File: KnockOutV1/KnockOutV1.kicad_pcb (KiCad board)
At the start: 2 copper layers, 1 part

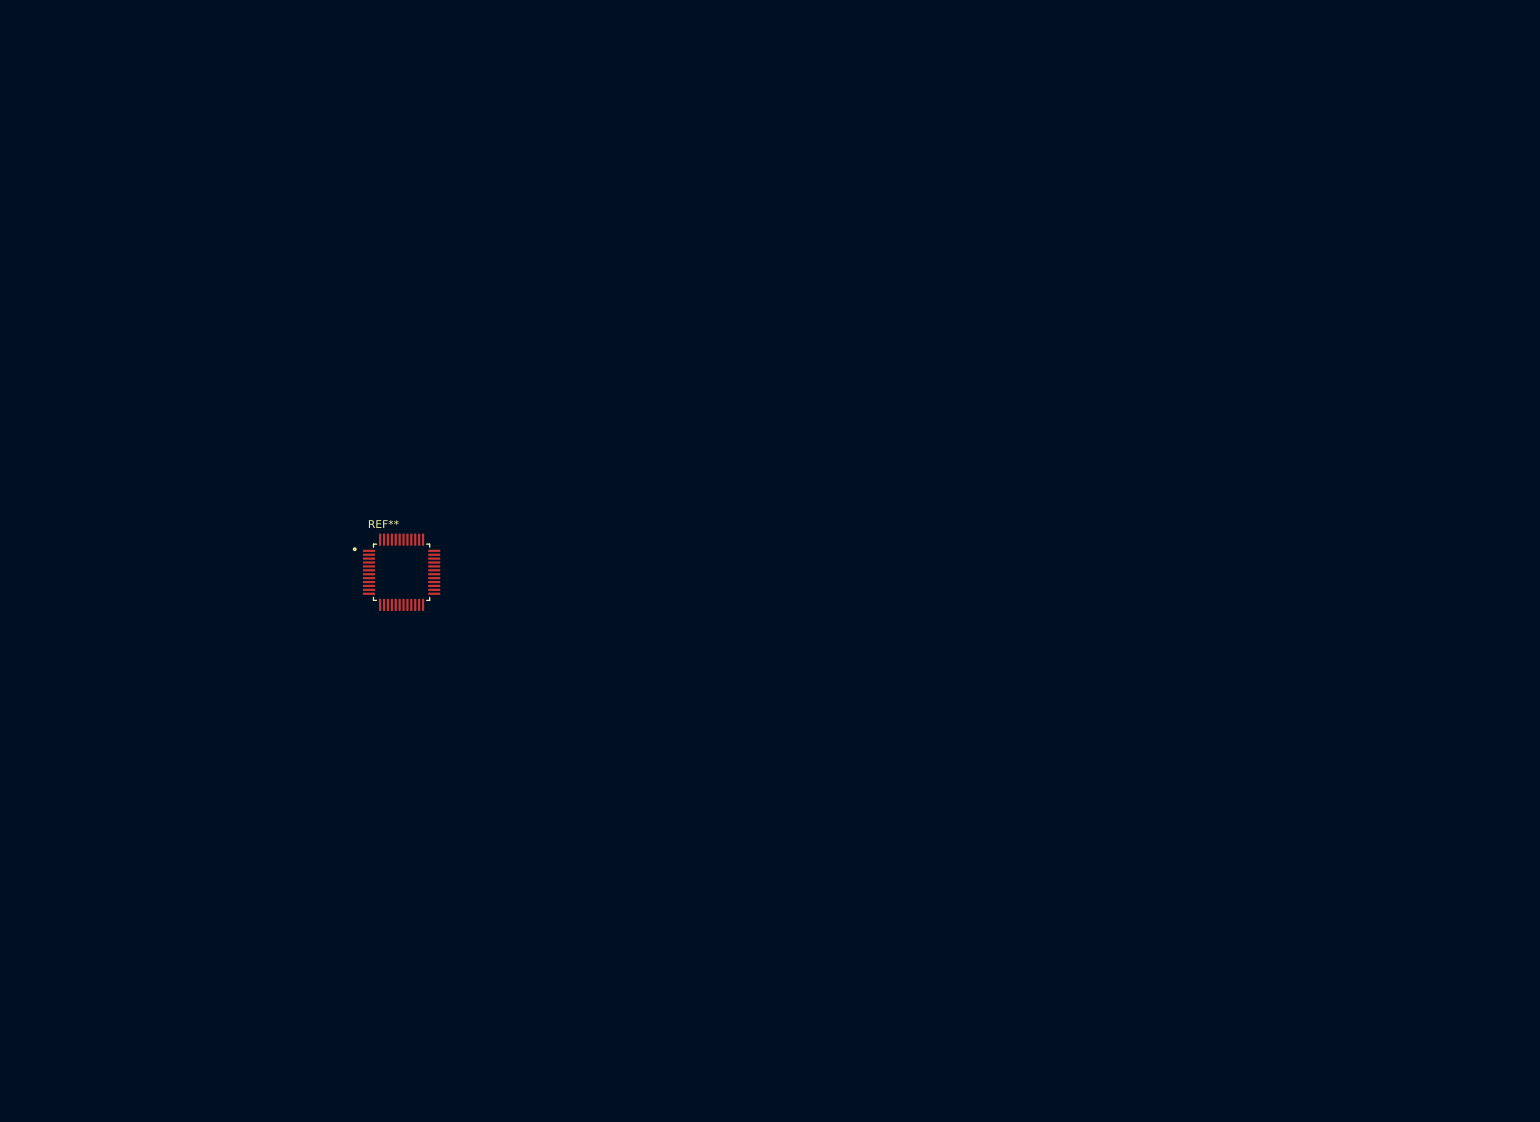
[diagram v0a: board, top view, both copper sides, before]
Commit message: Began Schematic Pin Breakout
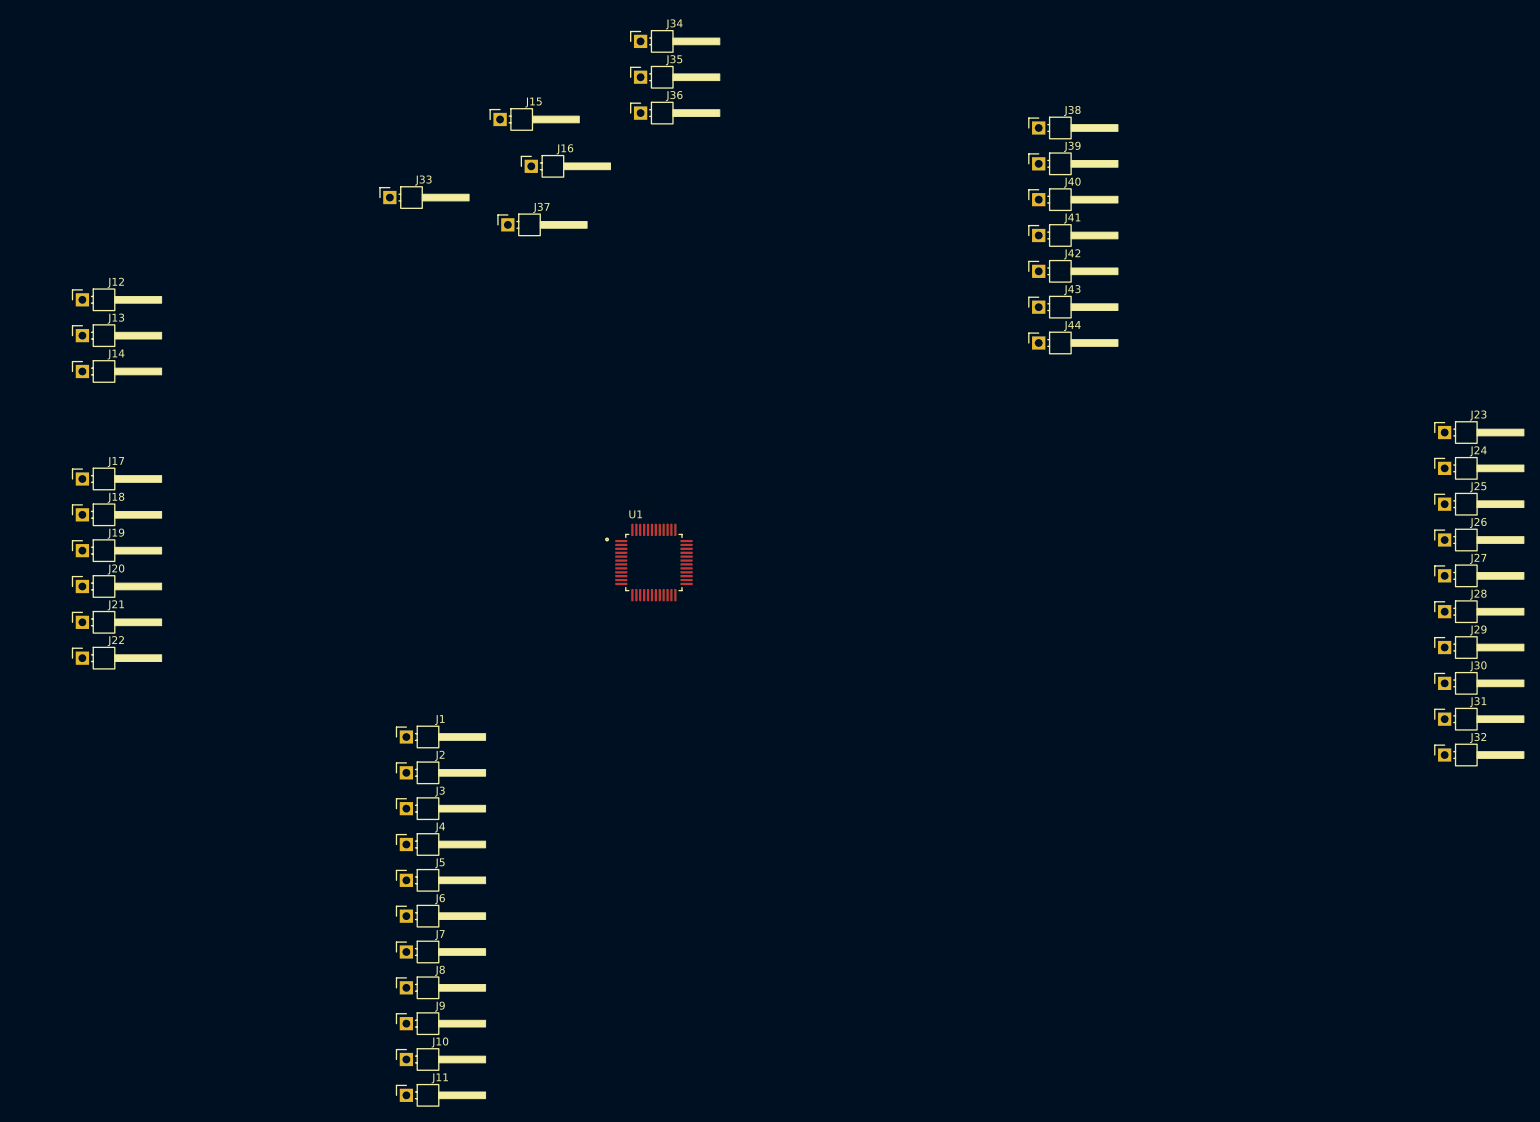
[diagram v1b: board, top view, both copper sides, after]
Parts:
- removed REF**: QFP50P900X900X160-48N, STM32F103C8T6:QFP50P900X900X160-48N
- added J1: Conn1x1Pin-PA0_WKUP, Connector_PinHeader_2.54mm:PinHeader_1x01_P2.54mm_Horizontal, F.Cu at (110.1, 109.6)
- added J10: Conn1x1Pin-PA9, Connector_PinHeader_2.54mm:PinHeader_1x01_P2.54mm_Horizontal, F.Cu at (110.1, 150.9)
- added J11: Conn1x1Pin-PA10, Connector_PinHeader_2.54mm:PinHeader_1x01_P2.54mm_Horizontal, F.Cu at (110.1, 155.5)
- added J12: Conn1x1Pin-PA11, Connector_PinHeader_2.54mm:PinHeader_1x01_P2.54mm_Horizontal, F.Cu at (68.6, 53.6)
- added J13: Conn1x1Pin-PA12, Connector_PinHeader_2.54mm:PinHeader_1x01_P2.54mm_Horizontal, F.Cu at (68.6, 58.2)
- added J14: Conn1x1Pin-PA13, Connector_PinHeader_2.54mm:PinHeader_1x01_P2.54mm_Horizontal, F.Cu at (68.6, 62.8)
- added J15: Conn1x1Pin-PA14, Connector_PinHeader_2.54mm:PinHeader_1x01_P2.54mm_Horizontal, F.Cu at (122.1, 30.5)
- added J16: Conn1x1Pin-PA15, Connector_PinHeader_2.54mm:PinHeader_1x01_P2.54mm_Horizontal, F.Cu at (126.1, 36.5)
- added J17: Conn1x1Pin-PC13-TAMPER-RTC, Connector_PinHeader_2.54mm:PinHeader_1x01_P2.54mm_Horizontal, F.Cu at (68.6, 76.5)
- added J18: Conn1x1Pin-PC14-OSC32_IN, Connector_PinHeader_2.54mm:PinHeader_1x01_P2.54mm_Horizontal, F.Cu at (68.6, 81.1)
- added J19: Conn1x1Pin-PC15-OSC32_OUT, Connector_PinHeader_2.54mm:PinHeader_1x01_P2.54mm_Horizontal, F.Cu at (68.6, 85.7)
- added J2: Conn1x1Pin-PA1, Connector_PinHeader_2.54mm:PinHeader_1x01_P2.54mm_Horizontal, F.Cu at (110.1, 114.2)
- added J20: Conn1x1Pin-VBAT, Connector_PinHeader_2.54mm:PinHeader_1x01_P2.54mm_Horizontal, F.Cu at (68.6, 90.3)
- added J21: Conn1x1Pin-NRST, Connector_PinHeader_2.54mm:PinHeader_1x01_P2.54mm_Horizontal, F.Cu at (68.6, 94.9)
- added J22: BOOT0, Connector_PinHeader_2.54mm:PinHeader_1x01_P2.54mm_Horizontal, F.Cu at (68.6, 99.5)
- added J23: Conn1x1Pin-VDD, Connector_PinHeader_2.54mm:PinHeader_1x01_P2.54mm_Horizontal, F.Cu at (243.1, 70.6)
- added J24: Conn1x1Pin-VDDA, Connector_PinHeader_2.54mm:PinHeader_1x01_P2.54mm_Horizontal, F.Cu at (243.1, 75.2)
- added J25: Conn1x1Pin-PB15, Connector_PinHeader_2.54mm:PinHeader_1x01_P2.54mm_Horizontal, F.Cu at (243.1, 79.8)
- added J26: Conn1x1Pin-PB14, Connector_PinHeader_2.54mm:PinHeader_1x01_P2.54mm_Horizontal, F.Cu at (243.1, 84.4)
- added J27: Conn1x1Pin-PB13, Connector_PinHeader_2.54mm:PinHeader_1x01_P2.54mm_Horizontal, F.Cu at (243.1, 89.0)
- added J28: Conn1x1Pin-PB12, Connector_PinHeader_2.54mm:PinHeader_1x01_P2.54mm_Horizontal, F.Cu at (243.1, 93.5)
- added J29: Conn1x1Pin-PB11, Connector_PinHeader_2.54mm:PinHeader_1x01_P2.54mm_Horizontal, F.Cu at (243.1, 98.1)
- added J3: Conn1x1Pin-PA2, Connector_PinHeader_2.54mm:PinHeader_1x01_P2.54mm_Horizontal, F.Cu at (110.1, 118.8)
- added J30: Conn1x1Pin-PB10, Connector_PinHeader_2.54mm:PinHeader_1x01_P2.54mm_Horizontal, F.Cu at (243.1, 102.7)
- added J31: Conn1x1Pin-PB9, Connector_PinHeader_2.54mm:PinHeader_1x01_P2.54mm_Horizontal, F.Cu at (243.1, 107.3)
- added J32: Conn1x1Pin-PB8, Connector_PinHeader_2.54mm:PinHeader_1x01_P2.54mm_Horizontal, F.Cu at (243.1, 111.9)
- added J33: Conn1x1Pin-PB7, Connector_PinHeader_2.54mm:PinHeader_1x01_P2.54mm_Horizontal, F.Cu at (108.0, 40.5)
- added J34: Conn1x1Pin-PB6, Connector_PinHeader_2.54mm:PinHeader_1x01_P2.54mm_Horizontal, F.Cu at (140.1, 20.5)
- added J35: Conn1x1Pin-PB5, Connector_PinHeader_2.54mm:PinHeader_1x01_P2.54mm_Horizontal, F.Cu at (140.1, 25.1)
- added J36: Conn1x1Pin-PB4, Connector_PinHeader_2.54mm:PinHeader_1x01_P2.54mm_Horizontal, F.Cu at (140.1, 29.7)
- added J37: Conn1x1Pin-PB3, Connector_PinHeader_2.54mm:PinHeader_1x01_P2.54mm_Horizontal, F.Cu at (123.1, 44.0)
- added J38: Conn1x1Pin-PB2, Connector_PinHeader_2.54mm:PinHeader_1x01_P2.54mm_Horizontal, F.Cu at (191.1, 31.6)
- added J39: Conn1x1Pin-PB1, Connector_PinHeader_2.54mm:PinHeader_1x01_P2.54mm_Horizontal, F.Cu at (191.1, 36.2)
- added J4: Conn1x1Pin-PA3, Connector_PinHeader_2.54mm:PinHeader_1x01_P2.54mm_Horizontal, F.Cu at (110.1, 123.4)
- added J40: Conn1x1Pin-PB0, Connector_PinHeader_2.54mm:PinHeader_1x01_P2.54mm_Horizontal, F.Cu at (191.1, 40.8)
- added J41: Conn1x1Pin-PC0_OSC_IN, Connector_PinHeader_2.54mm:PinHeader_1x01_P2.54mm_Horizontal, F.Cu at (191.1, 45.4)
- added J42: Conn1x1Pin-PD1_OSC_OUT, Connector_PinHeader_2.54mm:PinHeader_1x01_P2.54mm_Horizontal, F.Cu at (191.1, 50.0)
- added J43: Conn1x1Pin-VSSA, Connector_PinHeader_2.54mm:PinHeader_1x01_P2.54mm_Horizontal, F.Cu at (191.1, 54.5)
- added J44: Conn1x1Pin-VSS, Connector_PinHeader_2.54mm:PinHeader_1x01_P2.54mm_Horizontal, F.Cu at (191.1, 59.1)
- added J5: Conn1x1Pin-PA4, Connector_PinHeader_2.54mm:PinHeader_1x01_P2.54mm_Horizontal, F.Cu at (110.1, 128.0)
- added J6: Conn1x1Pin-PA5, Connector_PinHeader_2.54mm:PinHeader_1x01_P2.54mm_Horizontal, F.Cu at (110.1, 132.6)
- added J7: Conn1x1Pin-PA6, Connector_PinHeader_2.54mm:PinHeader_1x01_P2.54mm_Horizontal, F.Cu at (110.1, 137.1)
- added J8: Conn1x1Pin-PA7, Connector_PinHeader_2.54mm:PinHeader_1x01_P2.54mm_Horizontal, F.Cu at (110.1, 141.7)
- added J9: Conn1x1Pin-PA8, Connector_PinHeader_2.54mm:PinHeader_1x01_P2.54mm_Horizontal, F.Cu at (110.1, 146.3)
- added U1: STM32F103C8T6, STM32F103C8T6:QFP50P900X900X160-48N, F.Cu at (141.8, 87.2)

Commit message: PCB Pin Breakouts Finished
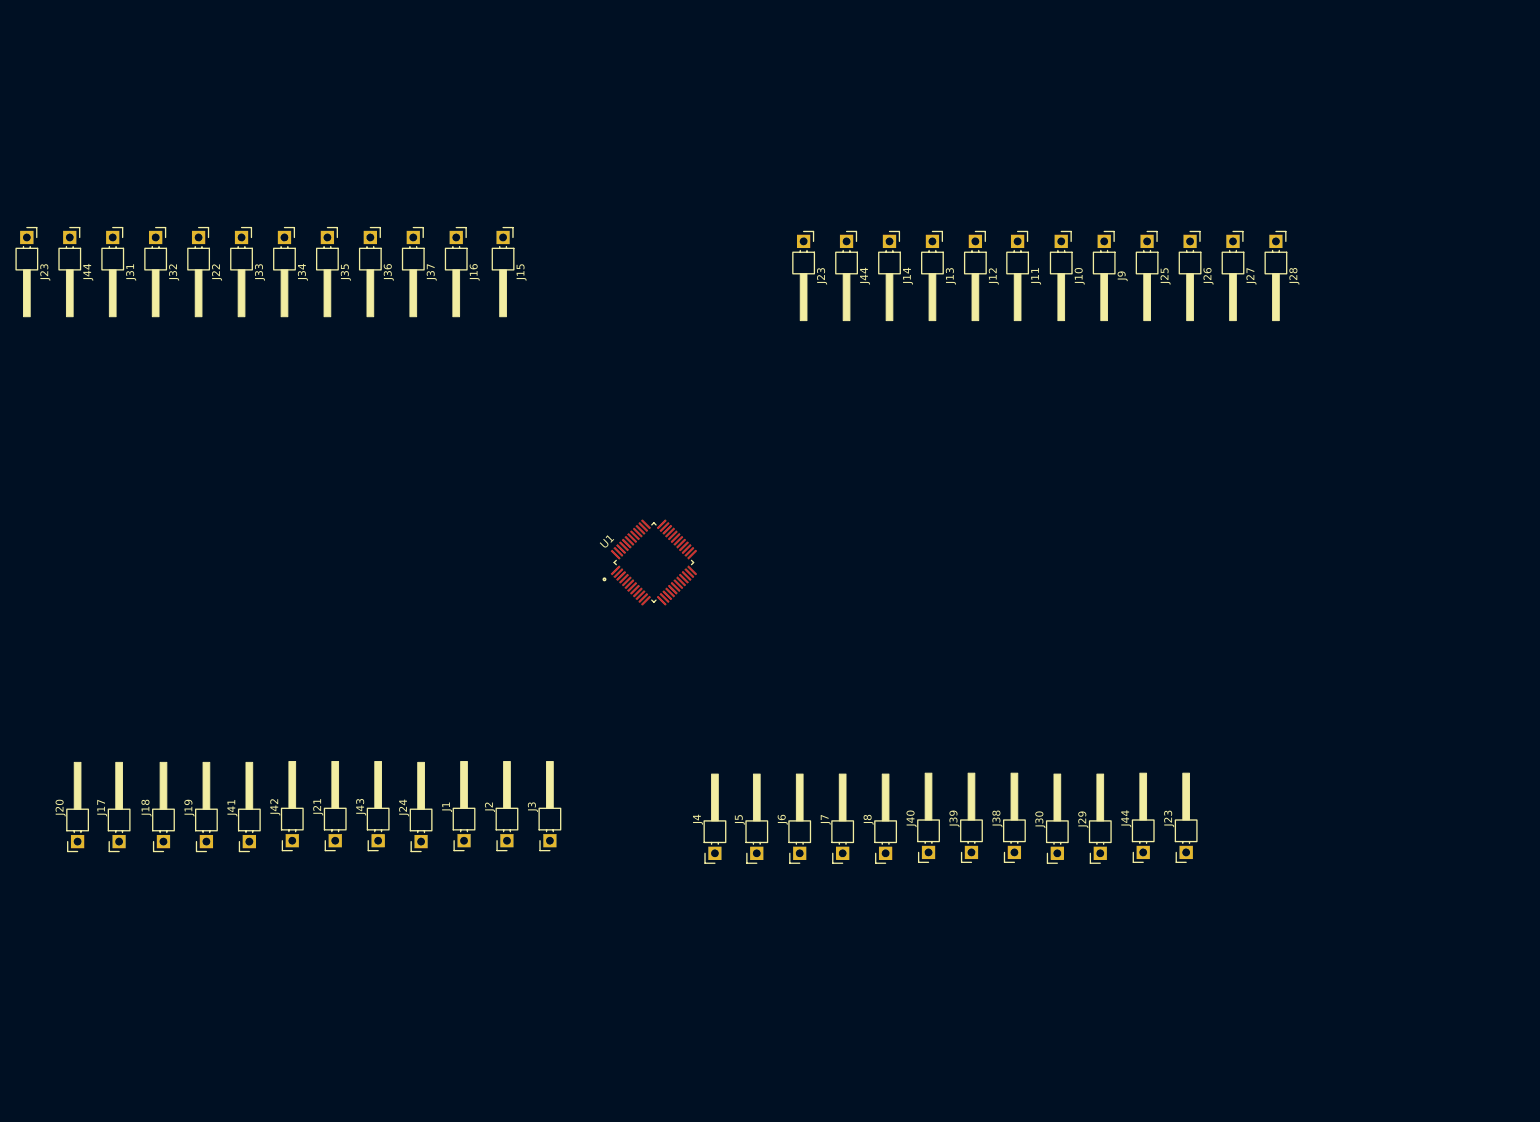
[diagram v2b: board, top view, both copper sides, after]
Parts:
- added J23: Conn1x1Pin-VDD, Connector_PinHeader_2.54mm:PinHeader_1x01_P2.54mm_Horizontal, F.Cu at (161.0, 46.1)
- added J23: Conn1x1Pin-VDD, Connector_PinHeader_2.54mm:PinHeader_1x01_P2.54mm_Horizontal, F.Cu at (210.0, 124.4)
- added J44: Conn1x1Pin-VSS, Connector_PinHeader_2.54mm:PinHeader_1x01_P2.54mm_Horizontal, F.Cu at (166.5, 46.1)
- added J44: Conn1x1Pin-VSS, Connector_PinHeader_2.54mm:PinHeader_1x01_P2.54mm_Horizontal, F.Cu at (204.5, 124.4)
- moved J23 183.3 mm to (61.5, 45.6), turned to -90 degrees
- moved J31 181.4 mm to (72.5, 45.6), turned to -90 degrees
- moved J32 177.9 mm to (78.0, 45.6), turned to -90 degrees
- moved J24 139.6 mm to (112.0, 123.0), turned to 90 degrees
- moved J11 134.5 mm to (188.4, 46.1), turned to -90 degrees
- moved J9 134.3 mm to (199.5, 46.1), turned to -90 degrees
- moved J10 134.2 mm to (194.0, 46.1), turned to -90 degrees
- moved J41 127.5 mm to (90.0, 123.0), turned to 90 degrees
- moved J44 124.8 mm to (67.0, 45.6), turned to -90 degrees
- moved J42 120.3 mm to (95.5, 122.9), turned to 90 degrees
- moved J12 114.6 mm to (183.0, 46.1), turned to -90 degrees
- moved J13 109.6 mm to (177.5, 46.1), turned to -90 degrees
- moved J43 108.8 mm to (106.5, 122.9), turned to 90 degrees
- moved J14 104.7 mm to (172.0, 46.1), turned to -90 degrees
- moved J38 92.8 mm to (188.0, 124.4), turned to 90 degrees
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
